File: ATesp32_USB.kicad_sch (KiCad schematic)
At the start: 18 parts, among them J1 USB_C_Receptacle_USB2.0_16P, U5 CP2102N-Axx-xQFN24

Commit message: first pass at footprint assignment
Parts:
- C15, C16, C17, C4: footprint (none) -> Capacitor_SMD:C_0603_1608Metric
- D5, D6: footprint (none) -> LED_SMD:LED_0603_1608Metric
- J1: footprint (none) -> Connector_USB:USB_C_Receptacle_G-Switch_GT-USB-7010ASV
- JP7, JP8: footprint (none) -> Jumper:SolderJumper-2_P1.3mm_Bridged_RoundedPad1.0x1.5mm
- R11, R12, R13, R14, R15, R5, R7: footprint (none) -> Resistor_SMD:R_0603_1608Metric
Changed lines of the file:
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@@
 			)
 		)
-		(property "Footprint" ""
+		(property "Footprint" "Resistor_SMD:R_0603_1608Metric"
 			(at 54.61 65.278 90)
 			(effects
@@
 			)
 		)
-		(property "Footprint" ""
+		(property "Footprint" "Resistor_SMD:R_0603_1608Metric"
 			(at 64.77 55.88 0)
 			(effects
@@
 			)
 		)
-		(property "Footprint" ""
+		(property "Footprint" "Capacitor_SMD:C_0603_1608Metric"
 			(at 103.8352 29.21 0)
 			(effects
@@
 			)
 		)
-		(property "Footprint" ""
+		(property "Footprint" "Jumper:SolderJumper-2_P1.3mm_Bridged_RoundedPad1.0x1.5mm"
 			(at 104.14 53.34 0)
 			(effects
@@
 			)
 		)
-		(property "Footprint" ""
+		(property "Footprint" "Connector_USB:USB_C_Receptacle_G-Switch_GT-USB-7010ASV"
 			(at 166.37 72.39 0)
 			(effects
@@
 			)
 		)
-		(property "Footprint" ""
+		(property "Footprint" "LED_SMD:LED_0603_1608Metric"
 			(at 105.41 92.71 90)
 			(effects
@@
 			)
 		)
-		(property "Footprint" ""
+		(property "Footprint" "Capacitor_SMD:C_0603_1608Metric"
 			(at 91.44 24.13 0)
 			(effects
@@
 			)
 		)
-		(property "Footprint" ""
+		(property "Footprint" "Resistor_SMD:R_0603_1608Metric"
 			(at 181.61 62.23 0)
 			(effects
@@
 			)
 		)
-		(property "Footprint" ""
+		(property "Footprint" "LED_SMD:LED_0603_1608Metric"
 			(at 119.38 97.79 90)
 			(effects
@@
 			)
 		)
-		(property "Footprint" ""
+		(property "Footprint" "Capacitor_SMD:C_0603_1608Metric"
 			(at 60.96 38.1 0)
 			(effects
@@
 			)
 		)
-		(property "Footprint" ""
+		(property "Footprint" "Resistor_SMD:R_0603_1608Metric"
 			(at 187.96 64.77 0)
 			(effects
@@
 			)
 		)
-		(property "Footprint" ""
+		(property "Footprint" "Jumper:SolderJumper-2_P1.3mm_Bridged_RoundedPad1.0x1.5mm"
 			(at 104.14 50.8 0)
 			(effects
@@
 			)
 		)
-		(property "Footprint" ""
+		(property "Footprint" "Capacitor_SMD:C_0603_1608Metric"
 			(at 73.3552 41.91 0)
 			(effects
@@
 			)
 		)
-		(property "Footprint" ""
+		(property "Footprint" "Resistor_SMD:R_0603_1608Metric"
 			(at 61.468 69.85 90)
 			(effects
@@
 			)
 		)
-		(property "Footprint" ""
+		(property "Footprint" "Resistor_SMD:R_0603_1608Metric"
 			(at 105.41 87.63 0)
 			(effects
@@
 			)
 		)
-		(property "Footprint" ""
+		(property "Footprint" "Resistor_SMD:R_0603_1608Metric"
 			(at 119.38 90.17 0)
 			(effects

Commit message: remove misc superfluous components
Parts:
- C15, C16, C17, C4: footprint Capacitor_SMD:C_0603_1608Metric -> Capacitor_SMD:C_0402_1005Metric
- D5, D6: footprint LED_SMD:LED_0603_1608Metric -> LED_SMD:LED_0402_1005Metric
- R11, R12, R13, R14, R15, R5, R7: footprint Resistor_SMD:R_0603_1608Metric -> Resistor_SMD:R_0402_1005Metric
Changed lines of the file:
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@@
 			)
 		)
-		(property "Footprint" "Resistor_SMD:R_0603_1608Metric"
+		(property "Footprint" "Resistor_SMD:R_0402_1005Metric"
 			(at 54.61 65.278 90)
 			(effects
@@
 			)
 		)
-		(property "Footprint" "Resistor_SMD:R_0603_1608Metric"
+		(property "Footprint" "Resistor_SMD:R_0402_1005Metric"
 			(at 64.77 55.88 0)
 			(effects
@@
 			)
 		)
-		(property "Footprint" "Capacitor_SMD:C_0603_1608Metric"
+		(property "Footprint" "Capacitor_SMD:C_0402_1005Metric"
 			(at 103.8352 29.21 0)
 			(effects
@@
 			)
 		)
-		(property "Footprint" "LED_SMD:LED_0603_1608Metric"
+		(property "Footprint" "LED_SMD:LED_0402_1005Metric"
 			(at 105.41 92.71 90)
 			(effects
@@
 			)
 		)
-		(property "Footprint" "Capacitor_SMD:C_0603_1608Metric"
+		(property "Footprint" "Capacitor_SMD:C_0402_1005Metric"
 			(at 91.44 24.13 0)
 			(effects
@@
 			)
 		)
-		(property "Footprint" "Resistor_SMD:R_0603_1608Metric"
+		(property "Footprint" "Resistor_SMD:R_0402_1005Metric"
 			(at 181.61 62.23 0)
 			(effects
@@
 			)
 		)
-		(property "Footprint" "LED_SMD:LED_0603_1608Metric"
+		(property "Footprint" "LED_SMD:LED_0402_1005Metric"
 			(at 119.38 97.79 90)
 			(effects
@@
 			)
 		)
-		(property "Footprint" "Capacitor_SMD:C_0603_1608Metric"
+		(property "Footprint" "Capacitor_SMD:C_0402_1005Metric"
 			(at 60.96 38.1 0)
 			(effects
@@
 			)
 		)
-		(property "Footprint" "Resistor_SMD:R_0603_1608Metric"
+		(property "Footprint" "Resistor_SMD:R_0402_1005Metric"
 			(at 187.96 64.77 0)
 			(effects
@@
 			)
 		)
-		(property "Footprint" "Capacitor_SMD:C_0603_1608Metric"
+		(property "Footprint" "Capacitor_SMD:C_0402_1005Metric"
 			(at 73.3552 41.91 0)
 			(effects
@@
 			)
 		)
-		(property "Footprint" "Resistor_SMD:R_0603_1608Metric"
+		(property "Footprint" "Resistor_SMD:R_0402_1005Metric"
 			(at 61.468 69.85 90)
 			(effects
@@
 			)
 		)
-		(property "Footprint" "Resistor_SMD:R_0603_1608Metric"
+		(property "Footprint" "Resistor_SMD:R_0402_1005Metric"
 			(at 105.41 87.63 0)
 			(effects
@@
 			)
 		)
-		(property "Footprint" "Resistor_SMD:R_0603_1608Metric"
+		(property "Footprint" "Resistor_SMD:R_0402_1005Metric"
 			(at 119.38 90.17 0)
 			(effects

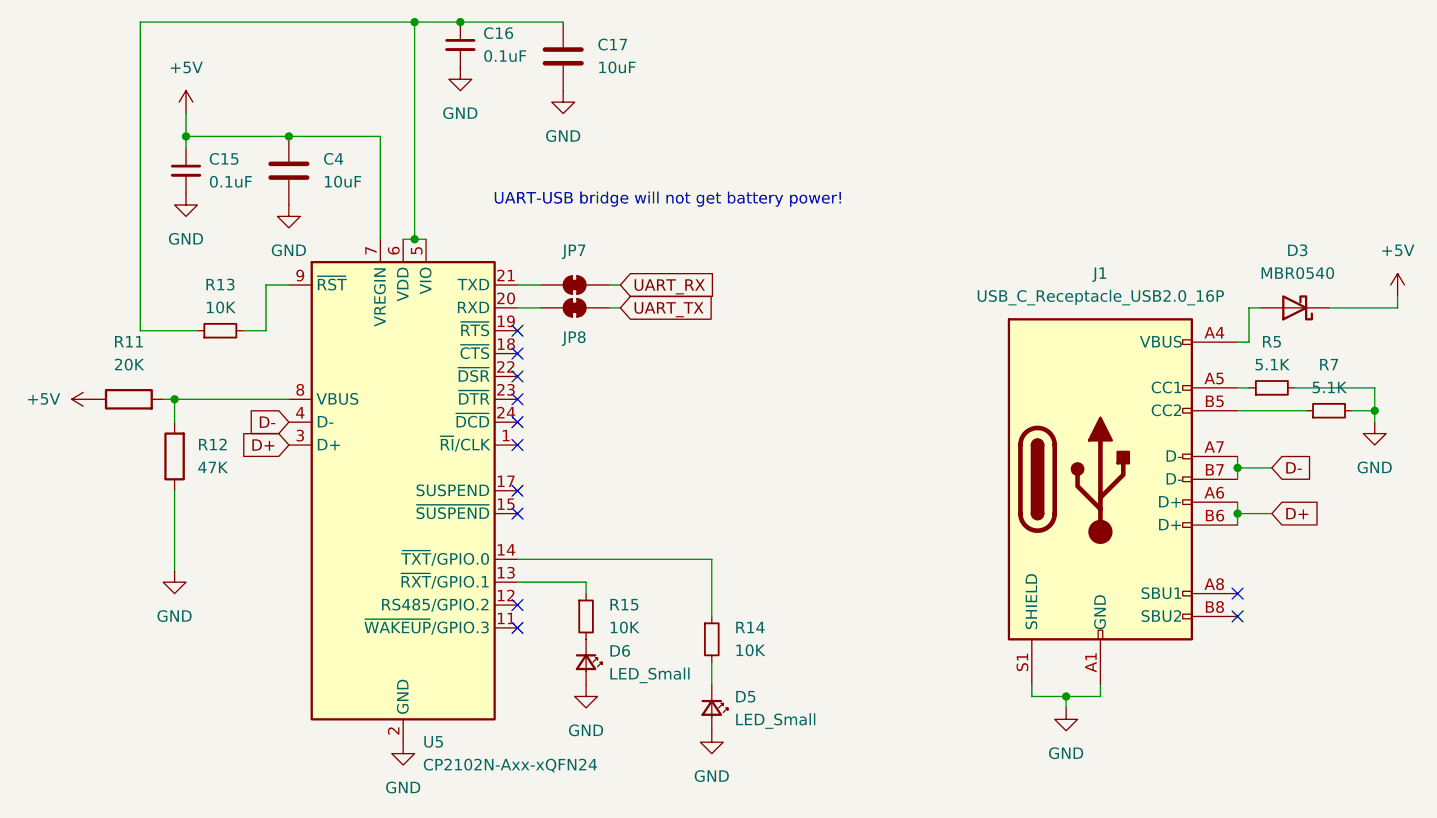
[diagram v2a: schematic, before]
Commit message: first pass at component placement
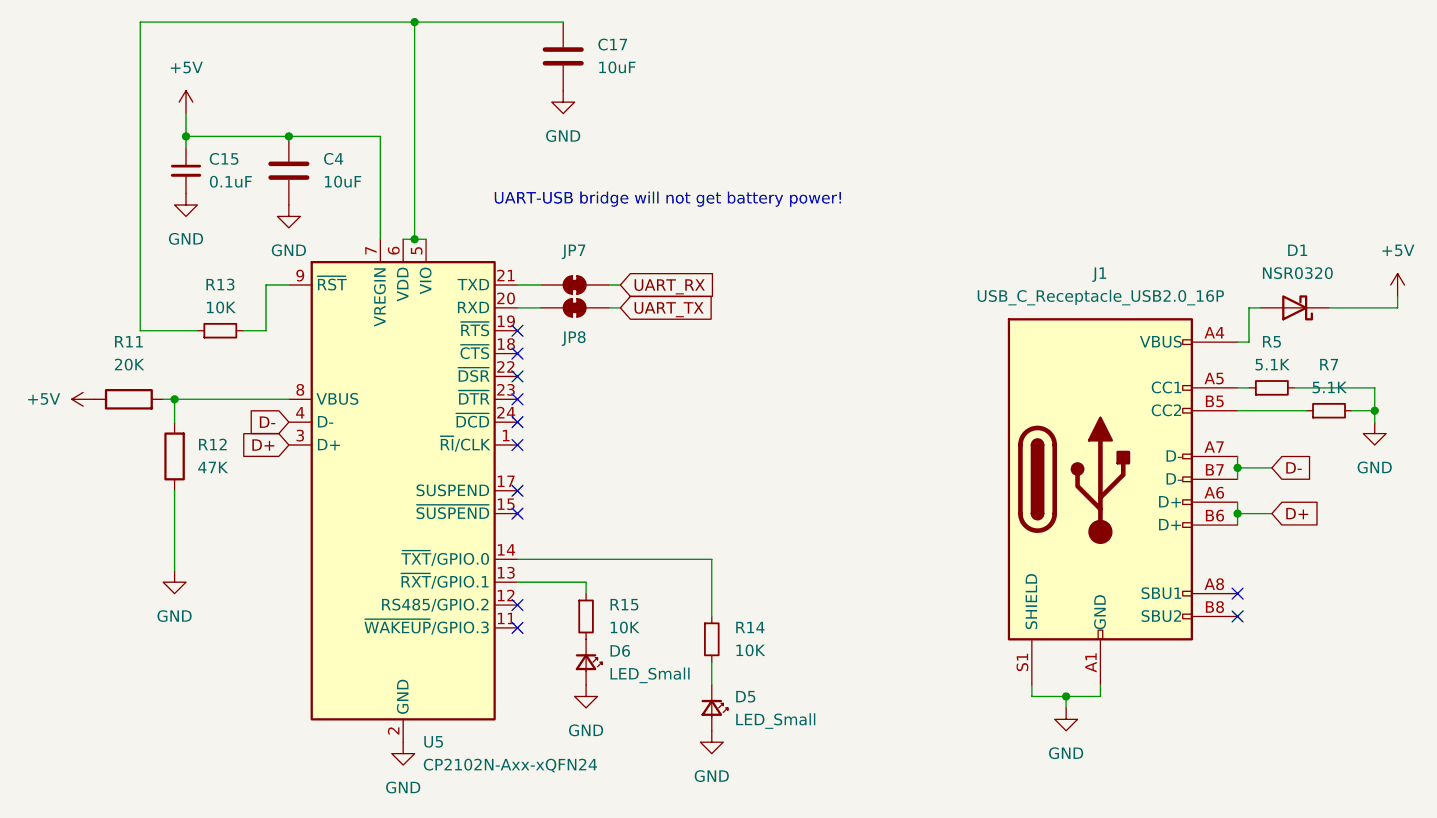
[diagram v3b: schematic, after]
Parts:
- removed C16: 0.1uF, Capacitor_SMD:C_0402_1005Metric, symbol Device:C_Small
- removed D3: MBR0540, Diode_SMD:D_SOD-123, symbol Diode:MBR0540
- added D1: NSR0320, Diode_SMD:D_SOD-323, symbol Diode:NSR0340HT1G
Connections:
- net +5V: now also D1.1 (K)
- net at J1.A4 (VBUS), J1.A9 (VBUS), J1.B4 (VBUS)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: now also D1.2 (A)

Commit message: satisfy DRC and ERC
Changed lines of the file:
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@@
+	)
+	(junction
+		(at 86.36 36.83)
+		(diameter 0)
+		(color 0 0 0 0)
 	)
 	(junction
@@
 	(wire
 		(pts
+			(xy 86.36 36.83) (xy 86.36 45.72)
+		)
+		(stroke
+			(width 0)
+			(type default)
+		)
+	)
+	(wire
+		(pts
 			(xy 86.36 45.72) (xy 87.63 45.72)
 		)
@@
 	(wire
 		(pts
-			(xy 86.36 21.59) (xy 86.36 45.72)
+			(xy 86.36 21.59) (xy 86.36 36.83)
 		)
 		(stroke
@@
 					(unit 1)
 				)
+			)
+		)
+	)
+	(symbol
+		(lib_id "power:PWR_FLAG")
+		(at 86.36 36.83 270)
+		(unit 1)
+		(exclude_from_sim no)
+		(in_bom yes)
+		(on_board yes)
+		(dnp no)
+		(fields_autoplaced yes)
+		(property "Reference" "#FLG01"
+			(at 88.265 36.83 0)
+			(effects
+				(font
+					(size 1.27 1.27)
+				)
+				(hide yes)
+			)
+		)
+		(property "Value" "PWR_FLAG"
+			(at 90.17 36.8299 90)
+			(effects
+				(font
+					(size 1.27 1.27)
+				)
+				(justify left)
+			)
+		)
+		(property "Footprint" ""
+			(at 86.36 36.83 0)
+			(effects
+				(font
+					(size 1.27 1.27)
+				)
+				(hide yes)
+			)
+		)
+		(property "Datasheet" "~"
+			(at 86.36 36.83 0)
+			(effects
+				(font
+					(size 1.27 1.27)
+				)
+				(hide yes)
+			)
+		)
+		(property "Description" "Special symbol for telling ERC where power comes from"
+			(at 86.36 36.83 0)
+			(effects
+				(font
+					(size 1.27 1.27)
+				)
+				(hide yes)
+			)
+		)
+		(pin "1"
+		)
+		(instances
+			(project ""
+				(path "/465ced44-ee36-4323-9fa6-a4501ea89ff6/200b673f-247f-42e9-b156-337638e0ff82"
+					(reference "#FLG01")
+					(unit 1)
+				)

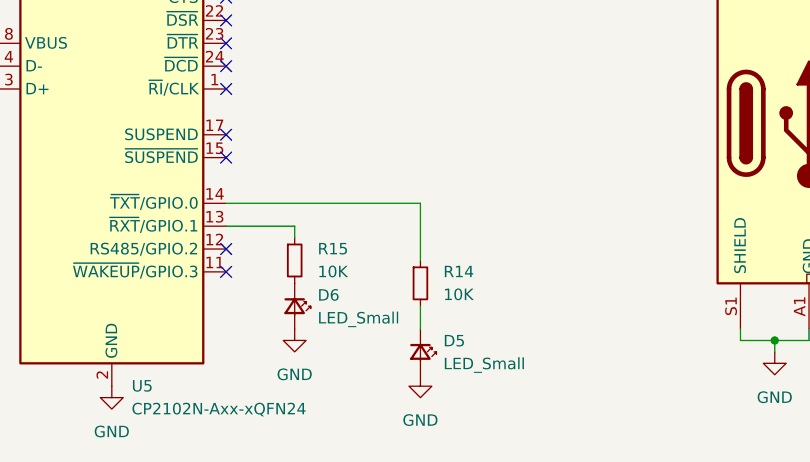
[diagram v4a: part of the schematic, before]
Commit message: spec components for JLC
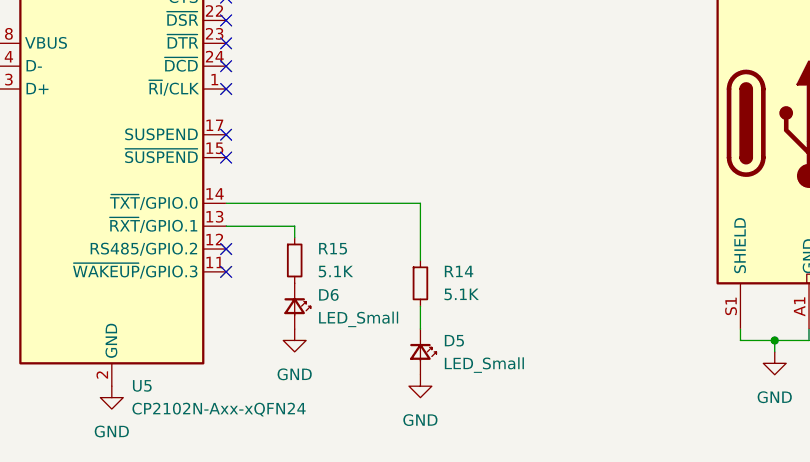
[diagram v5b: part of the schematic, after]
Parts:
- C15: JLC (none) -> C1525
- C17, C4: JLC (none) -> C315248
- D1: JLC (none) -> C48192
- D5, D6: JLC (none) -> C510300
- J1: JLC (none) -> C2988369
- R11: JLC (none) -> C25765
- R12: JLC (none) -> C25792
- R13: JLC (none) -> C25744
- R14, R15: value 10K -> 5.1K; JLC (none) -> C25905
- R5, R7: JLC (none) -> C25905
- U5: JLC (none) -> C969151

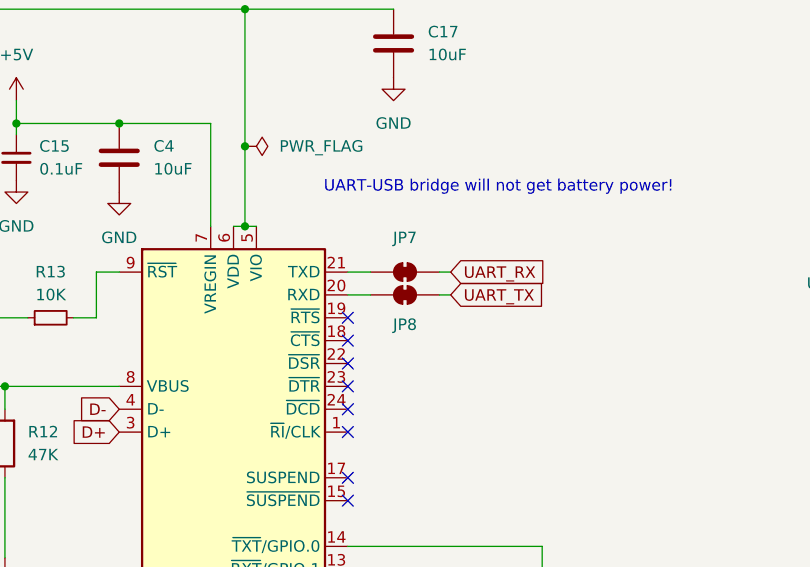
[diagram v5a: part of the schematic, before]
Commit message: Generate production files. More clear part names for ESP and LiPo charger
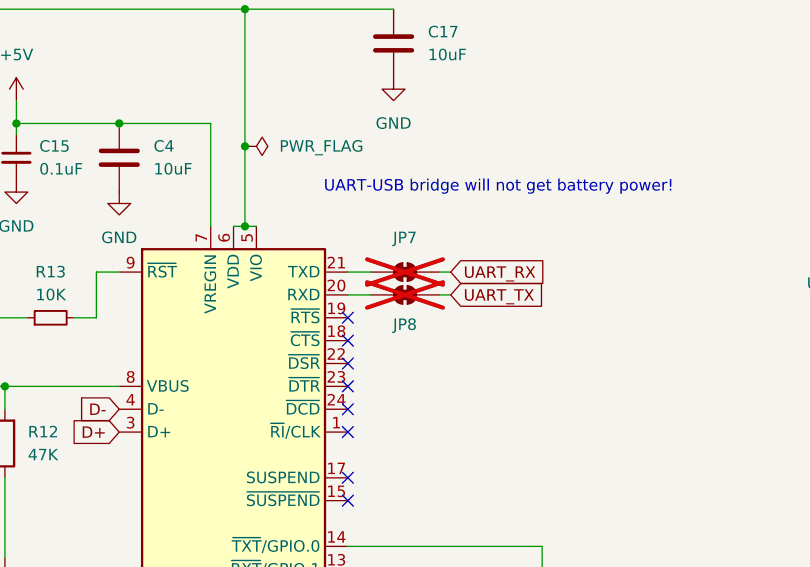
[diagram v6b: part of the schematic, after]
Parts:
- JP7, JP8: now not fitted
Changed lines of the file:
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@@
 		(in_bom no)
 		(on_board yes)
-		(dnp no)
+		(dnp yes)
 		(property "Reference" "JP8"
 			(at 104.14 56.642 0)
@@
 		(in_bom no)
 		(on_board yes)
-		(dnp no)
+		(dnp yes)
 		(fields_autoplaced yes)
 		(property "Reference" "JP7"

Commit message: generated manf files. Too damn expensive, adjusting min track and holes
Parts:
- C15: JLC C1525 -> (none); LCSC (none) -> C1525
- C17, C4: JLC C315248 -> (none); LCSC (none) -> C315248
- D1: JLC C48192 -> (none); LCSC (none) -> C48192
- D5, D6: JLC C510300 -> (none); LCSC (none) -> C510300
- J1: JLC C2988369 -> (none); LCSC (none) -> C2988369
- R11: JLC C25765 -> (none); LCSC (none) -> C25765
- R12: JLC C25792 -> (none); LCSC (none) -> C25792
- R13: JLC C25744 -> (none); LCSC (none) -> C25744
- R14, R15, R5, R7: JLC C25905 -> (none); LCSC (none) -> C25905
- U5: JLC C969151 -> (none); LCSC (none) -> C969151
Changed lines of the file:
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@@
 			)
 		)
-		(property "JLC" "C25765"
+		(property "LCSC" "C25765"
 			(at 54.61 63.5 0)
 			(effects
@@
 			)
 		)
-		(property "JLC" "C48192"
+		(property "LCSC" "C48192"
 			(at 184.15 53.34 0)
 			(effects
@@
 			)
 		)
-		(property "JLC" "C25744"
+		(property "LCSC" "C25744"
 			(at 64.77 55.88 0)
 			(effects
@@
 			)
 		)
-		(property "JLC" "C315248"
-			(at 102.87 25.4 0)
-			(effects
-				(font
-					(size 1.27 1.27)
-				)
-				(hide yes)
-			)
-		)
 		(property "Sim.Device" ""
 			(at 102.87 25.4 0)
@@
 		)
 		(property "Sim.Type" ""
+			(at 102.87 25.4 0)
+			(effects
+				(font
+					(size 1.27 1.27)
+				)
+				(hide yes)
+			)
+		)
+		(property "LCSC" "C315248"
 			(at 102.87 25.4 0)
 			(effects
@@
 			)
 		)
-		(property "JLC" "C2988369"
+		(property "LCSC" "C2988369"
 			(at 162.56 72.39 0)
 			(effects
@@
 			)
 		)
-		(property "JLC" "C510300"
+		(property "LCSC" "C510300"
 			(at 105.41 92.71 0)
 			(effects
@@
 			)
 		)
-		(property "JLC" "C25905"
+		(property "LCSC" "C25905"
 			(at 181.61 62.23 0)
 			(effects
@@
 			)
 		)
-		(property "JLC" "C510300"
+		(property "LCSC" "C510300"
 			(at 119.38 97.79 0)
 			(effects
@@
 			)
 		)
-		(property "JLC" "C1525"
-			(at 60.96 38.1 0)
-			(effects
-				(font
-					(size 1.27 1.27)
-				)
-				(hide yes)
-			)
-		)
 		(property "Sim.Device" ""
 			(at 60.96 38.1 0)
@@
 		)
 		(property "Sim.Type" ""
+			(at 60.96 38.1 0)
+			(effects
+				(font
+					(size 1.27 1.27)
+				)
+				(hide yes)
+			)
+		)
+		(property "LCSC" "C1525"
 			(at 60.96 38.1 0)
 			(effects
@@
 			)
 		)
-		(property "JLC" "C25905"
+		(property "LCSC" "C25905"
 			(at 187.96 64.77 0)
 			(effects
@@
 			)
 		)
-		(property "JLC" "C969151"
+		(property "LCSC" "C969151"
 			(at 85.09 73.66 0)
 			(effects
@@
 			)
 		)
-		(property "JLC" "C315248"
-			(at 72.39 38.1 0)
-			(effects
-				(font
-					(size 1.27 1.27)
-				)
-				(hide yes)
-			)
-		)
 		(property "Sim.Device" ""
 			(at 72.39 38.1 0)
@@
 		)
 		(property "Sim.Type" ""
+			(at 72.39 38.1 0)
+			(effects
+				(font
+					(size 1.27 1.27)
+				)
+				(hide yes)
+			)
+		)
+		(property "LCSC" "C315248"
 			(at 72.39 38.1 0)
 			(effects
@@
 			)
 		)
-		(property "JLC" "C25792"
+		(property "LCSC" "C25792"
 			(at 59.69 69.85 0)
 			(effects
@@
 			)
 		)
-		(property "JLC" "C25905"
+		(property "LCSC" "C25905"
 			(at 105.41 87.63 0)
 			(effects
@@
 			)
 		)
-		(property "JLC" "C25905"
+		(property "LCSC" "C25905"
 			(at 119.38 90.17 0)
 			(effects

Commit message: Add some Mouser PNs
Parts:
- C15: DigiKey (none) -> 1276-1001-1-ND; Mouser (none) -> 187-CL05B104KO5NNNC
- C17, C4: DigiKey (none) -> 1276-1450-1-ND
- D1: DigiKey (none) -> NSR0320MW2T1GOSCT-ND
- D5, D6: DigiKey (none) -> SML-P11UTT86RCT-ND
- J1: footprint Connector_USB:USB_C_Receptacle_G-Switch_GT-USB-7010ASV -> Connector_USB:USB_C_Receptacle_GCT_USB4105-xx-A_16P_TopMnt_Horizontal; DigiKey (none) -> 2073-USB4105-GF-ACT-ND
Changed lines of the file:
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@@
+			)
+		)
+		(property "DigiKey" "NSR0320MW2T1GOSCT-ND"
+			(at 184.15 53.34 0)
+			(effects
+				(font
+					(size 1.27 1.27)
+				)
+				(hide yes)
 			)
 		)
@@
 			)
 		)
+		(property "DigiKey" "1276-1450-1-ND"
+			(at 102.87 25.4 0)
+			(effects
+				(font
+					(size 1.27 1.27)
+				)
+				(hide yes)
+			)
+		)
 		(pin "1"
 		)
@@
 			)
 		)
-		(property "Footprint" "Connector_USB:USB_C_Receptacle_G-Switch_GT-USB-7010ASV"
+		(property "Footprint" "Connector_USB:USB_C_Receptacle_GCT_USB4105-xx-A_16P_TopMnt_Horizontal"
 			(at 166.37 72.39 0)
 			(effects
@@
 		)
 		(property "LCSC" "C2988369"
+			(at 162.56 72.39 0)
+			(effects
+				(font
+					(size 1.27 1.27)
+				)
+				(hide yes)
+			)
+		)
+		(property "DigiKey" "2073-USB4105-GF-ACT-ND"
 			(at 162.56 72.39 0)
 			(effects
@@
 			)
 		)
+		(property "DigiKey" "SML-P11UTT86RCT-ND"
+			(at 105.41 92.71 0)
+			(effects
+				(font
+					(size 1.27 1.27)
+				)
+				(hide yes)
+			)
+		)
 		(pin "1"
 		)
@@
 			)
 		)
+		(property "DigiKey" "SML-P11UTT86RCT-ND"
+			(at 119.38 97.79 0)
+			(effects
+				(font
+					(size 1.27 1.27)
+				)
+				(hide yes)
+			)
+		)
 		(pin "1"
 		)
@@
 			)
 		)
+		(property "DigiKey" "1276-1001-1-ND"
+			(at 60.96 38.1 0)
+			(effects
+				(font
+					(size 1.27 1.27)
+				)
+				(hide yes)
+			)
+		)
+		(property "Mouser" "187-CL05B104KO5NNNC"
+			(at 60.96 38.1 0)
+			(effects
+				(font
+					(size 1.27 1.27)
+				)
+				(hide yes)
+			)
+		)
 		(pin "1"
 		)
@@
 			(at 72.39 38.1 0)
 			(effects
+				(font
+					(size 1.27 1.27)
+				)
+				(hide yes)
+			)
+		)
+		(property "DigiKey" "1276-1450-1-ND"
+			(at 72.39 38.1 0)
+			(effects
